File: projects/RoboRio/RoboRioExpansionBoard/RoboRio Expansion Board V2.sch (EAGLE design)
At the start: 121 parts, among them J1 RRINTERFACE-FEMALE, J10 SPI_MISO, J12 I2C_SCL, J13 I2C_SDA, J14 UART_TX, J15 UART_RX, J16 LCD, J2 MICROSD-HINGED, J24 TP_GND, J25 PWM0, J26 PWM1, J27 PWM2, J28 PWM3, J29 PWM4, J3 51387-0578, J30 PWM5, J31 PWM6, J32 PWM7, J33 PWM8, J34 PWM9, J35 AI0, J36 AI1, J37 AI2, J38 AI3, J39 AO0, J40 AO1, J8 SPI_CS, J9 SPI_CLK, Q1 NPN-SOT416, Q2 NPN-SOT416, Q3 NPN-SOT416, U1 P8X32A-Q44_P, U2 24LC256ST, U3 FT232RL, U4 TC54-CB, U5 TPS2115APWR, U6 REG1117, U7 ADC124S01, U8 ADC124S01, Y1 HC\49USCRYSTAL

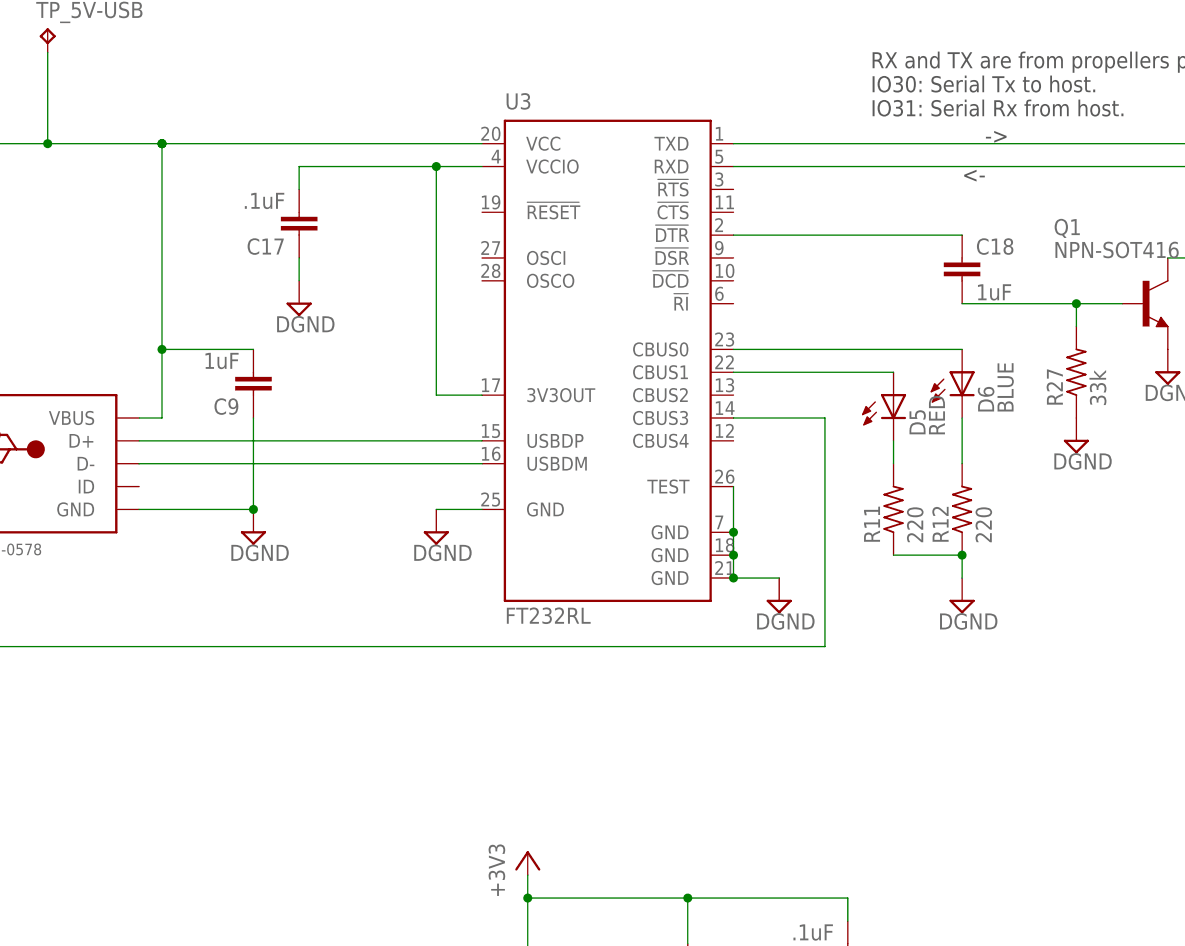
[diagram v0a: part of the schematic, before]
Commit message: Changed Circuitry for LED's on CBUS pins for FT232
Also added the symbol for the FT231X FT232RL replacement
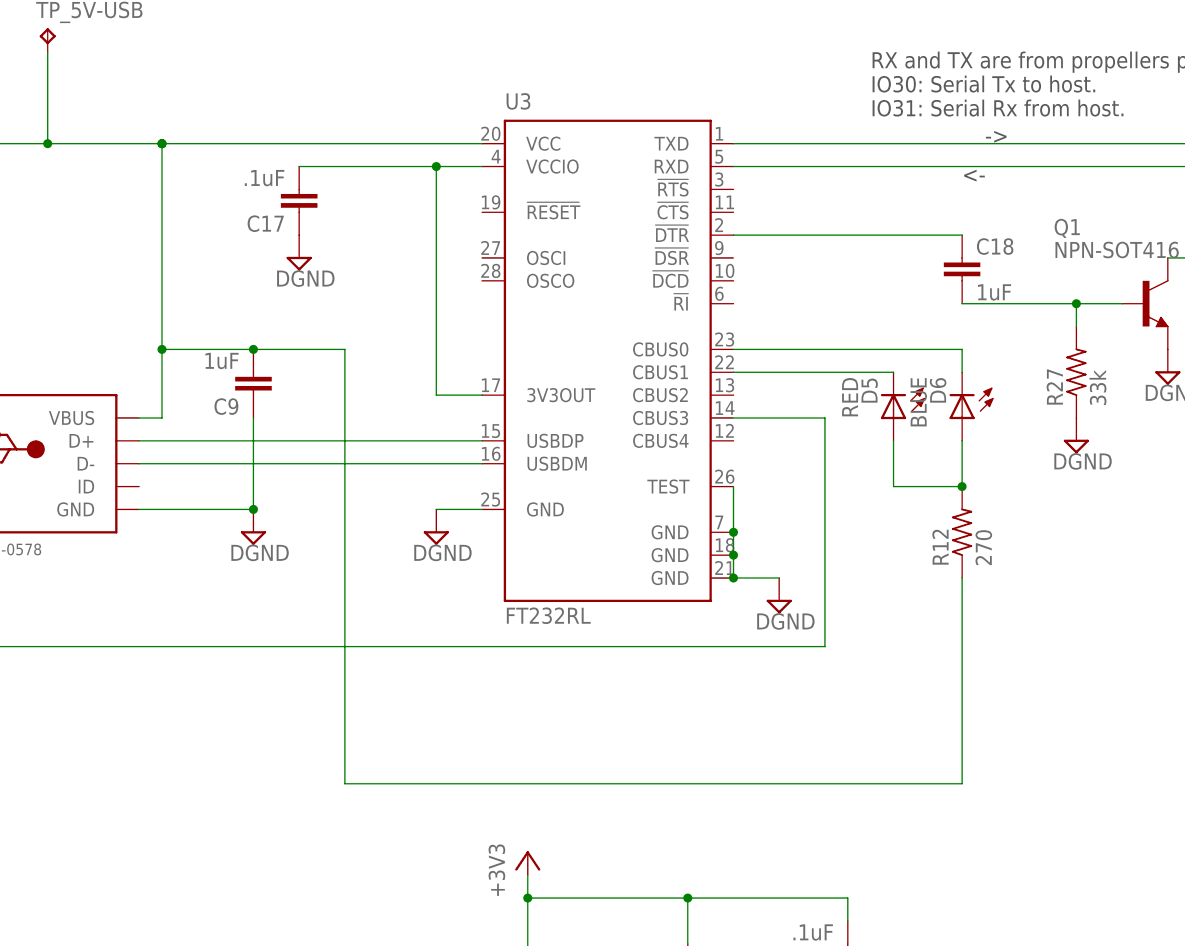
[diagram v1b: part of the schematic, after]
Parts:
- removed R11: 220, resistor:R-US_R0603
- R12: value 220 -> 270
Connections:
- removed net N$18: D6.C, R12.2
- removed net N$27: D6.A, U3.CBUS0
- removed net N$28: D5.A, U3.CBUS1
- new net N$17: D5.A, D6.A, R12.2
- new net N$6: D6.C, U3.CBUS0
- net 5VUSB: now also R12.1
- net DGND: no longer R11.1, R12.1
- net N$7: now also U3.CBUS1; no longer R11.2
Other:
- moved on the sheet: C17, D5, D6, R12

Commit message: Revert "Changed Circuitry for LED's on CBUS pins for FT232"
This reverts commit 5790a9f9b9c9d846d253dddb61c6fedc17bde5e4.
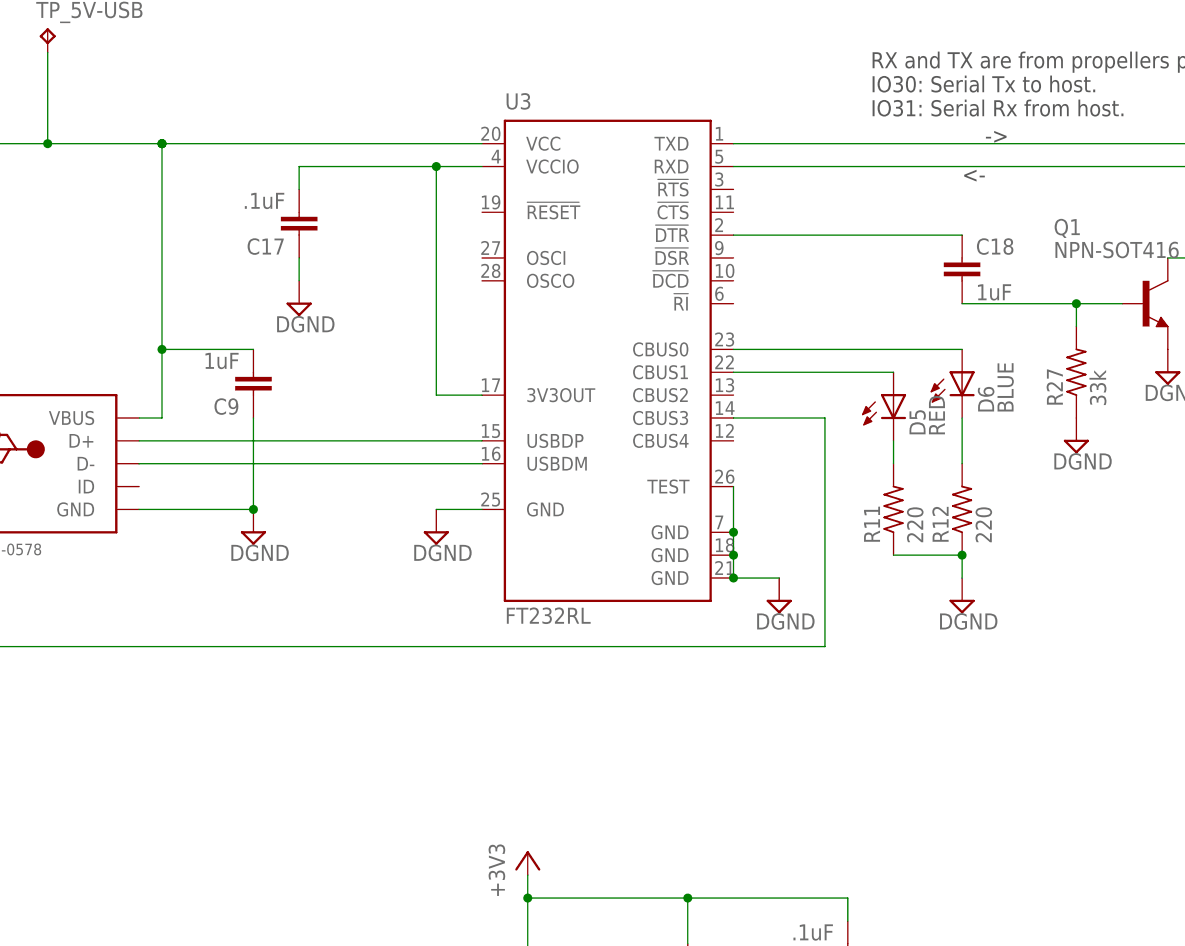
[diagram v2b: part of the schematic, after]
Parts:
- added R11: 220, resistor:R-US_R0603
- R12: value 270 -> 220
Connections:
- removed net N$17: D5.A, D6.A, R12.2
- removed net N$6: D6.C, U3.CBUS0
- new net N$18: D6.C, R12.2
- new net N$27: D6.A, U3.CBUS0
- new net N$28: D5.A, U3.CBUS1
- net 5VUSB: no longer R12.1
- net DGND: now also R11.1, R12.1
- net N$7: now also R11.2; no longer U3.CBUS1
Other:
- moved on the sheet: C17, D5, D6, R12

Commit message: Lots of stuff
I didn't sync before starting, meaning I crashed github. Now fixed via
manual save-as, but don't remember everything that was done. Sorry.
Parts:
- added D7: RED, led:LEDCHIPLED_0603
- added R36: 270, resistor:R-US_R0603
- C18: value 1uF -> .1uF
- D2: value YELLOW -> GREEN
- D3: value RED -> GREEN
- J11: value (none) -> SPI_MOSI
- R10, R11, R12, R4, R9: value 220 -> 270
- R27: value 33k -> 10K
- Y1: value HC\49USCRYSTAL -> 5MHz
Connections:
- removed net N$27: D6.A, U3.CBUS0
- removed net N$28: D5.A, U3.CBUS1
- new net N$17: D7.A, R36.2
- new net N$23: D6.A, R12.2
- new net N$6: D6.C, U3.CBUS0
- net 5VUSB: now also R11.1, R12.1
- net DGND: now also D7.C; no longer R11.1, R12.1
- net IO26: now also R36.1
- net N$18: now also D5.A, R11.2; no longer D6.C, R12.2
- net N$7: now also U3.CBUS1; no longer R11.2
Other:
- note added: "Internal Pullup"
- moved on the sheet: C18, D1, D2, D3, D5, D6, Q1, R10, R12, R27, R4, R9

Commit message: Set ADC power supplys to 3v, added bypass caps
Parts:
- added C25, C26, C27: .1uF, resistor:C-EUC0603K
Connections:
- net +3V3: now also C26.1, J17.V+, J18.V+, J19.V+, J20.V+, J21.V+, J22.V+, J23.V+
- net +5V: no longer J17.V+, J18.V+, J19.V+, J20.V+, J21.V+, J22.V+, J23.V+
- net DGND: now also C26.2
- net GND: now also C25.2, C27.2
- net VA: now also C25.1, C27.1

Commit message: Schematic notes
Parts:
- U4: value TC54-CB -> TC54VN43
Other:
- note added: "(4.21 to 4.39)"
- note added: "Vth = 4.3V nominal"
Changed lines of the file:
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@@
 <part name="SUPPLY1" library="supply2" deviceset="DGND" device=""/>
 <part name="R5" library="resistor" deviceset="R-US_" device="R0603" value="1k"/>
-<part name="U4" library="m-pad-2.1" deviceset="TC54" device="-CB"/>
+<part name="U4" library="m-pad-2.1" deviceset="TC54" device="-CB" value="TC54VN43"/>
 <part name="U6" library="burr-brown" deviceset="REG1117" device="">
 <attribute name="MPN" value="AP1117"/>
@@
 IO31: Serial Rx from host.</text>
 <text x="-27.94" y="-27.94" size="1.778" layer="97">Internal Pullup</text>
+<text x="-106.68" y="187.96" size="1.778" layer="97">Vth = 4.3V nominal</text>
+<text x="-106.68" y="185.42" size="1.778" layer="97">(4.21 to 4.39)</text>
 </plain>
 <instances>

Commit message: Updated USB connector
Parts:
- J3: device adafruit:USBMINIB -> adafruit:USB
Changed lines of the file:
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@@
 <grid distance="0.1" unitdist="inch" unit="inch" style="lines" multiple="1" display="no" altdistance="0.05" altunitdist="inch" altunit="inch"/>
 <layers>
-<layer number="1" name="Top" color="4" fill="1" visible="no" active="no"/>
-<layer number="16" name="Bottom" color="1" fill="1" visible="no" active="no"/>
-<layer number="17" name="Pads" color="2" fill="1" visible="no" active="no"/>
-<layer number="18" name="Vias" color="2" fill="1" visible="no" active="no"/>
-<layer number="19" name="Unrouted" color="6" fill="1" visible="no" active="no"/>
-<layer number="20" name="Dimension" color="15" fill="1" visible="no" active="no"/>
-<layer number="21" name="tPlace" color="7" fill="1" visible="no" active="no"/>
-<layer number="22" name="bPlace" color="7" fill="1" visible="no" active="no"/>
-<layer number="23" name="tOrigins" color="15" fill="1" visible="no" active="no"/>
-<layer number="24" name="bOrigins" color="15" fill="1" visible="no" active="no"/>
-<layer number="25" name="tNames" color="7" fill="1" visible="no" active="no"/>
-<layer number="26" name="bNames" color="7" fill="1" visible="no" active="no"/>
-<layer number="27" name="tValues" color="7" fill="1" visible="no" active="no"/>
-<layer number="28" name="bValues" color="7" fill="1" visible="no" active="no"/>
+<layer number="1" name="Top" color="4" fill="1" visible="yes" active="no"/>
+<layer number="16" name="Bottom" color="1" fill="1" visible="yes" active="no"/>
+<layer number="17" name="Pads" color="2" fill="1" visible="yes" active="no"/>
+<layer number="18" name="Vias" color="2" fill="1" visible="yes" active="no"/>
+<layer number="19" name="Unrouted" color="6" fill="1" visible="yes" active="no"/>
+<layer number="20" name="Dimension" color="15" fill="1" visible="yes" active="no"/>
+<layer number="21" name="tPlace" color="7" fill="1" visible="yes" active="no"/>
+<layer number="22" name="bPlace" color="7" fill="1" visible="yes" active="no"/>
+<layer number="23" name="tOrigins" color="15" fill="1" visible="yes" active="no"/>
+<layer number="24" name="bOrigins" color="15" fill="1" visible="yes" active="no"/>
+<layer number="25" name="tNames" color="7" fill="1" visible="yes" active="no"/>
+<layer number="26" name="bNames" color="7" fill="1" visible="yes" active="no"/>
+<layer number="27" name="tValues" color="7" fill="1" visible="yes" active="no"/>
+<layer number="28" name="bValues" color="7" fill="1" visible="yes" active="no"/>
 <layer number="29" name="tStop" color="7" fill="3" visible="no" active="no"/>
 <layer number="30" name="bStop" color="7" fill="6" visible="no" active="no"/>
@@
 <layer number="35" name="tGlue" color="7" fill="4" visible="no" active="no"/>
 <layer number="36" name="bGlue" color="7" fill="5" visible="no" active="no"/>
-<layer number="37" name="tTest" color="7" fill="1" visible="no" active="no"/>
-<layer number="38" name="bTest" color="7" fill="1" visible="no" active="no"/>
+<layer number="37" name="tTest" color="7" fill="1" visible="yes" active="no"/>
+<layer number="38" name="bTest" color="7" fill="1" visible="yes" active="no"/>
 <layer number="39" name="tKeepout" color="4" fill="11" visible="no" active="no"/>
 <layer number="40" name="bKeepout" color="1" fill="11" visible="no" active="no"/>
@@
 <layer number="44" name="Drills" color="7" fill="1" visible="no" active="no"/>
 <layer number="45" name="Holes" color="7" fill="1" visible="no" active="no"/>
-<layer number="46" name="Milling" color="3" fill="1" visible="no" active="no"/>
-<layer number="47" name="Measures" color="7" fill="1" visible="no" active="no"/>
-<layer number="48" name="Document" color="7" fill="1" visible="no" active="no"/>
-<layer number="49" name="Reference" color="7" fill="1" visible="no" active="no"/>
-<layer number="50" name="dxf" color="7" fill="1" visible="no" active="no"/>
-<layer number="51" name="tDocu" color="7" fill="1" visible="no" active="no"/>
-<layer number="52" name="bDocu" color="7" fill="1" visible="no" active="no"/>
-<layer number="53" name="tGND_GNDA" color="7" fill="9" visible="no" active="no"/>
-<layer number="54" name="bGND_GNDA" color="1" fill="9" visible="no" active="no"/>
-<layer number="56" name="wert" color="7" fill="1" visible="no" active="no"/>
-<layer number="57" name="tCAD" color="7" fill="1" visible="no" active="no"/>
+<layer number="46" name="Milling" color="3" fill="1" visible="yes" active="no"/>
+<layer number="47" name="Measures" color="7" fill="1" visible="yes" active="no"/>
+<layer number="48" name="Document" color="7" fill="1" visible="yes" active="no"/>
+<layer number="49" name="Reference" color="7" fill="1" visible="yes" active="no"/>
+<layer number="50" name="dxf" color="7" fill="1" visible="yes" active="no"/>
+<layer number="51" name="tDocu" color="7" fill="1" visible="yes" active="no"/>
+<layer number="52" name="bDocu" color="7" fill="1" visible="yes" active="no"/>
+<layer number="53" name="tGND_GNDA" color="7" fill="9" visible="yes" active="no"/>
+<layer number="54" name="bGND_GNDA" color="1" fill="9" visible="yes" active="no"/>
+<layer number="56" name="wert" color="7" fill="1" visible="yes" active="no"/>
+<layer number="57" name="tCAD" color="7" fill="1" visible="yes" active="no"/>
 <layer number="90" name="Modules" color="5" fill="1" visible="yes" active="yes"/>
 <layer number="91" name="Nets" color="2" fill="1" visible="yes" active="yes"/>
@@
 <part name="R33" library="resistor" deviceset="R-US_" device="R0603" value="10k"/>
 <part name="R34" library="resistor" deviceset="R-US_" device="R0603" value="10k"/>
-<part name="J3" library="adafruit" deviceset="USB" device="MINIB" value="51387-0578"/>
+<part name="J3" library="adafruit" deviceset="USB" device="" value="51387-0578"/>
 <part name="C9" library="resistor" deviceset="C-EU" device="C0603K" value="1uF"/>
 <part name="J25" library="3pin" deviceset="3PINDEVICE" device="DEFAULT" value="PWM0"/>
